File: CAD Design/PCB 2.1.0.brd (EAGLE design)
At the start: 100 x 80 mm, 55 parts, among them U1 CC2538, U2 MAX1555, X1 32MHz, X2 FC-12M

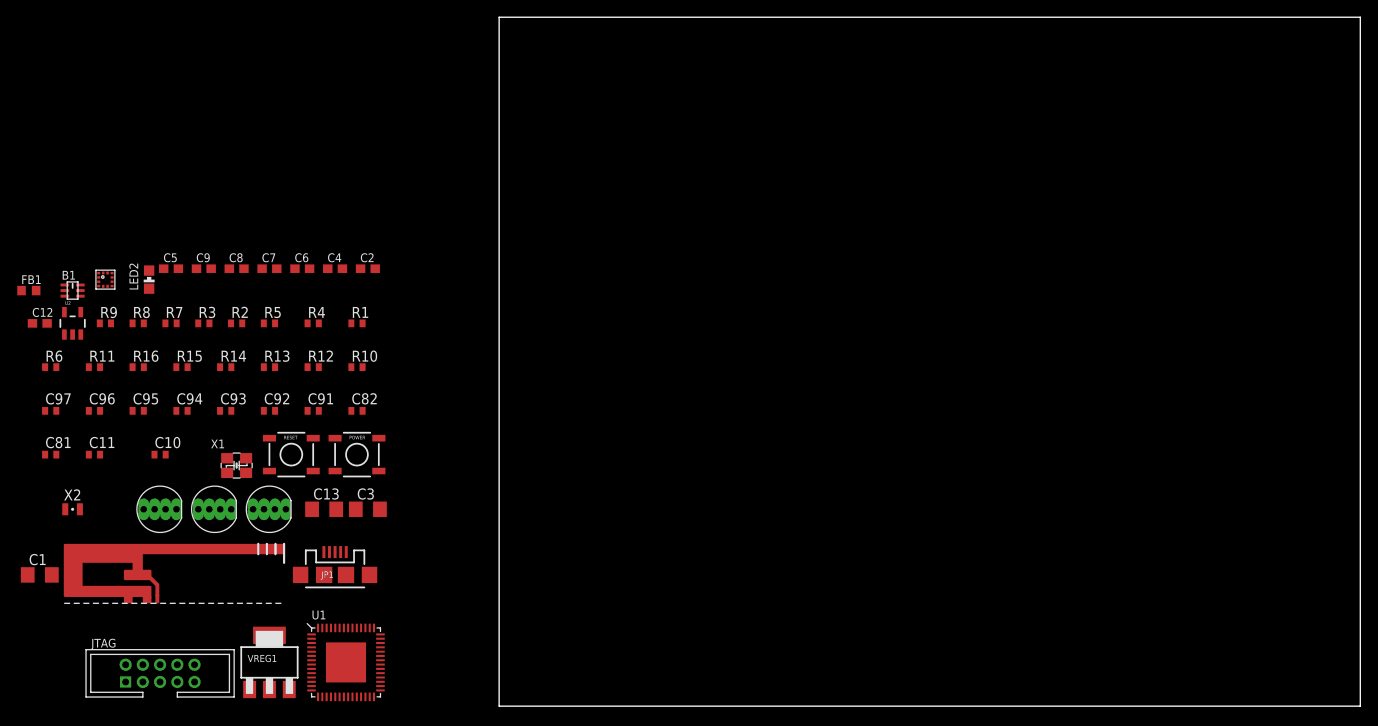
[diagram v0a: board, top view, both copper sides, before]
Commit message: Schematic Update, board push
Replaced some capacitors, 2.1 board with preliminary element placement
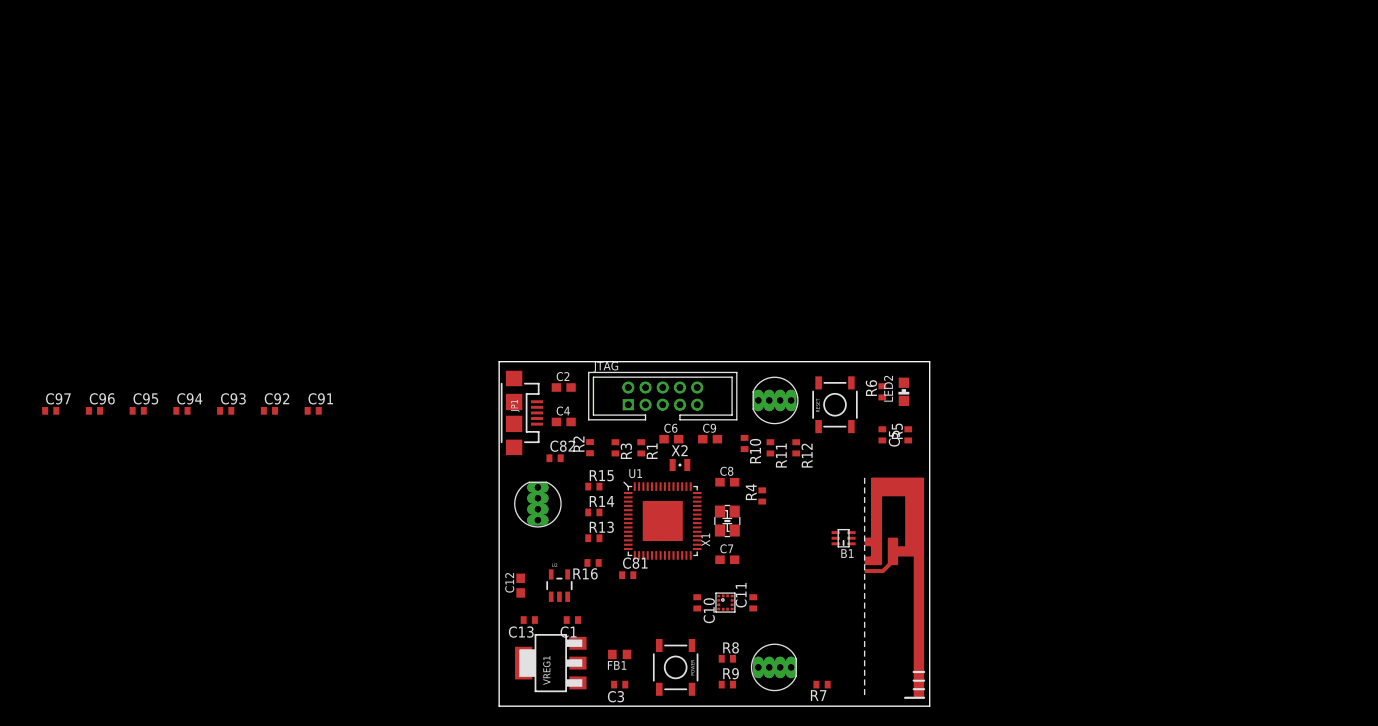
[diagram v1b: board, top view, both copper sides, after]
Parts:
- C1, C13, C3: device discrete:C1206 -> discrete:C0402
- C5: device discrete:C0603 -> discrete:C0402
- moved R6 96.6 mm to (44.5, 36.5), turned to 90 degrees
- moved B1 94.0 mm to (40.0, 19.5), turned to 180 degrees
- moved LED2 88.6 mm to (47.0, 36.5)
- moved U$2 87.7 mm to (45.7, 17.9), turned to 270 degrees
- moved R7 86.5 mm to (37.5, 2.50), turned to 180 degrees
- moved C5 84.8 mm to (44.5, 31.5), turned to 270 degrees
- moved R9 83.5 mm to (26.5, 2.50)
- moved U$1 81.2 mm to (26.3, 12.0)
- moved FB1 80.6 mm to (14.0, 6.00), turned to 180 degrees
- moved R11 79.0 mm to (31.5, 30.0), turned to 270 degrees
- moved R8 78.7 mm to (26.5, 5.50)
- moved C11 78.4 mm to (29.5, 12.0), turned to 90 degrees
- moved R5 75.3 mm to (47.5, 31.5), turned to 90 degrees
- moved D4 72.5 mm to (32.0, 35.5), turned to 180 degrees
- moved X2 70.7 mm to (21.0, 28.0)
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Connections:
- net GND: now also C1.2; no longer C1.1
- net N$14: now also C1.1; no longer C1.2
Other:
- board size 100 x 80 mm -> 50 x 40 mm
